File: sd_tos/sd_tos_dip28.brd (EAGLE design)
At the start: 19.5 x 63.5 mm, 20 parts, among them IC1 MEGA16-A, IC3 74HCT595D

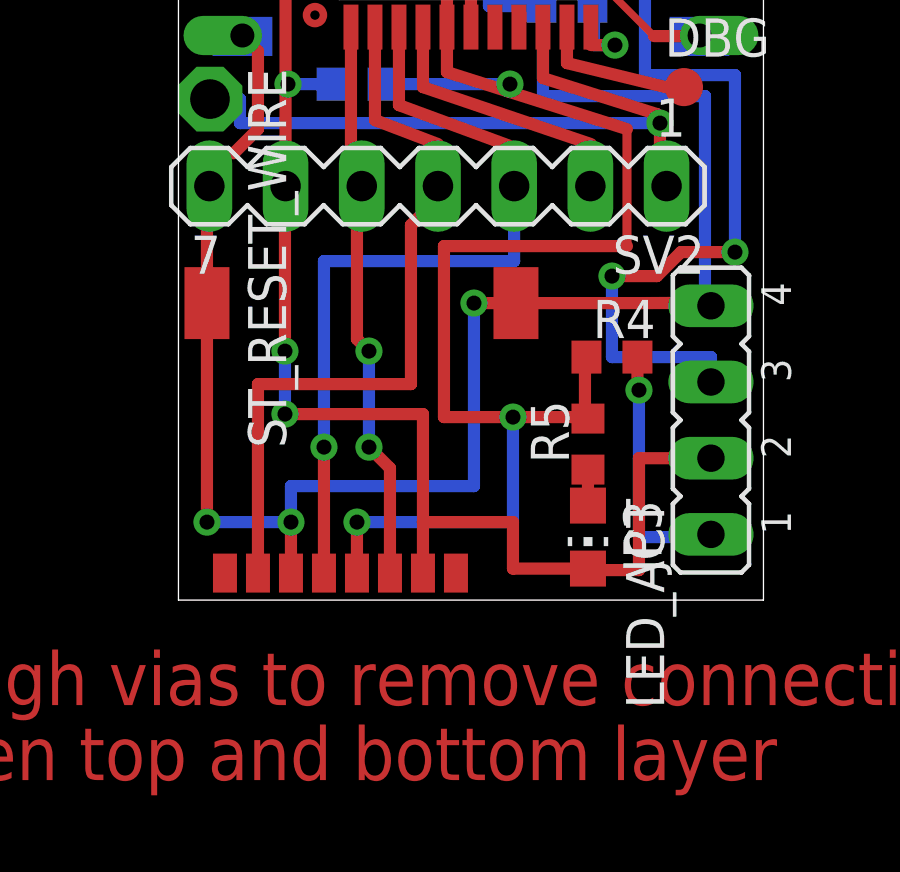
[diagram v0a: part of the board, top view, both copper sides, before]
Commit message: micro sd connector altered to match the real one
git-svn-id: https://subversion.assembla.com/svn/atarijookie/trunk@941 0d2ca917-fb58-4453-bb26-a698c01b0940
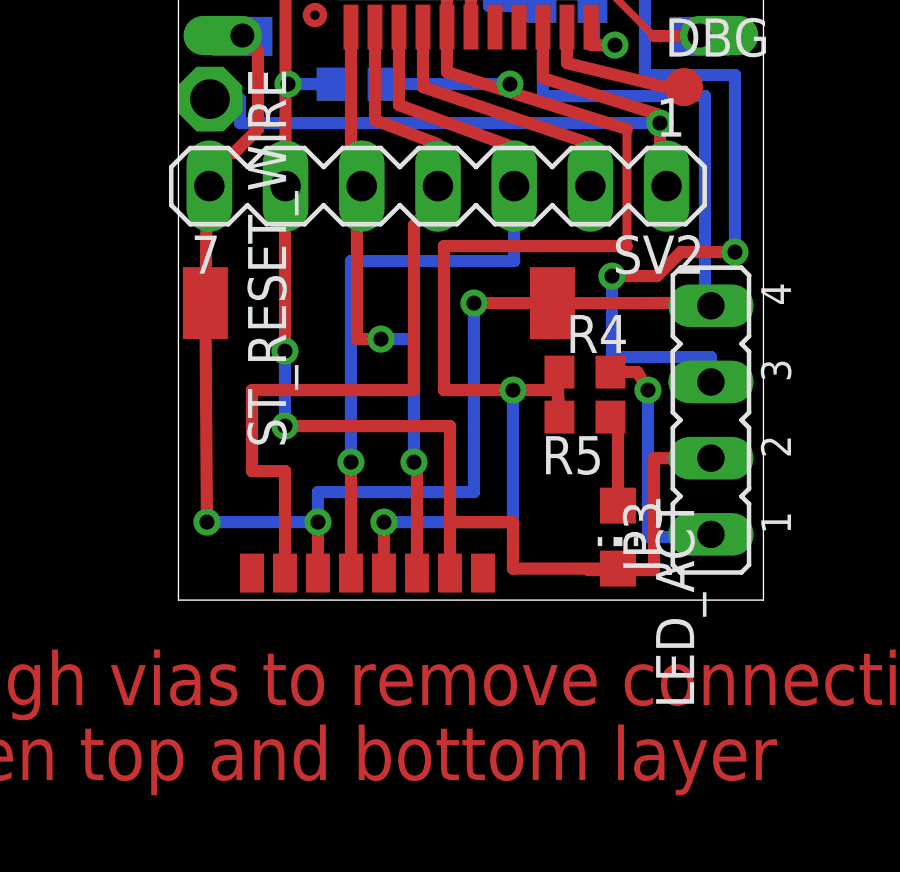
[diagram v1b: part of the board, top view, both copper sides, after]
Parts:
- moved R4 1.03 mm to (48.3, 11.6)
- moved LED_ACT 1.00 mm to (49.4, 6.10)
- moved R5 0.91 mm to (48.3, 10.1), turned to 180 degrees
- moved U$3 0.90 mm to (41.6, 4.90)
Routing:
- net N$2: track 1.20 -> 3.20 mm
- net SD_CS: track 41.5 -> 43.5 mm
- net VCC: track 167.5 -> 166.0 mm
- net MOSI: track 19.0 -> 20.5 mm
- net MISO: track 25.1 -> 26.5 mm
- net SCK: track 27.2 -> 26.3 mm
